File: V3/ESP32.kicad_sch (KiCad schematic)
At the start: 21 parts

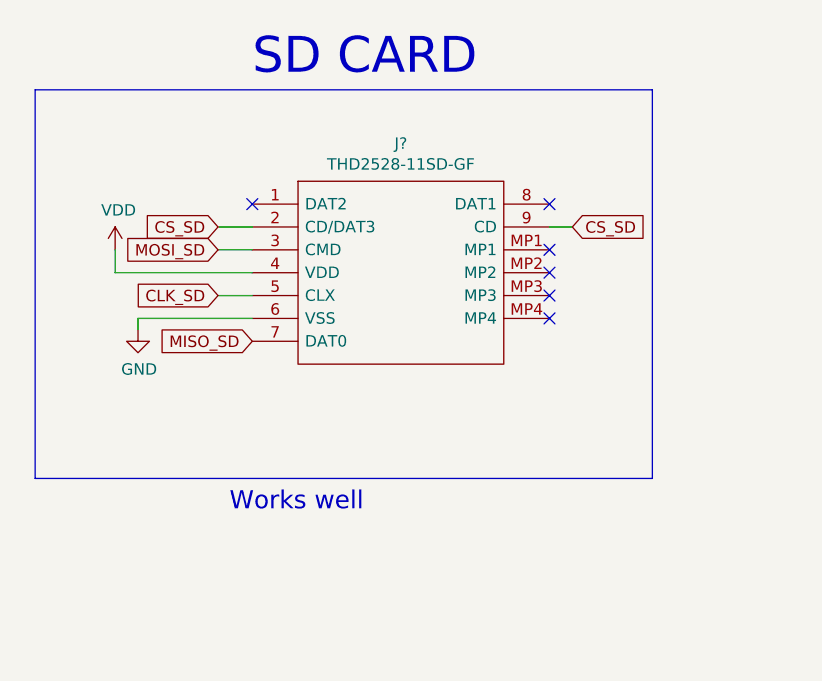
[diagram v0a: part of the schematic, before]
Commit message: Changed imu added flash chip
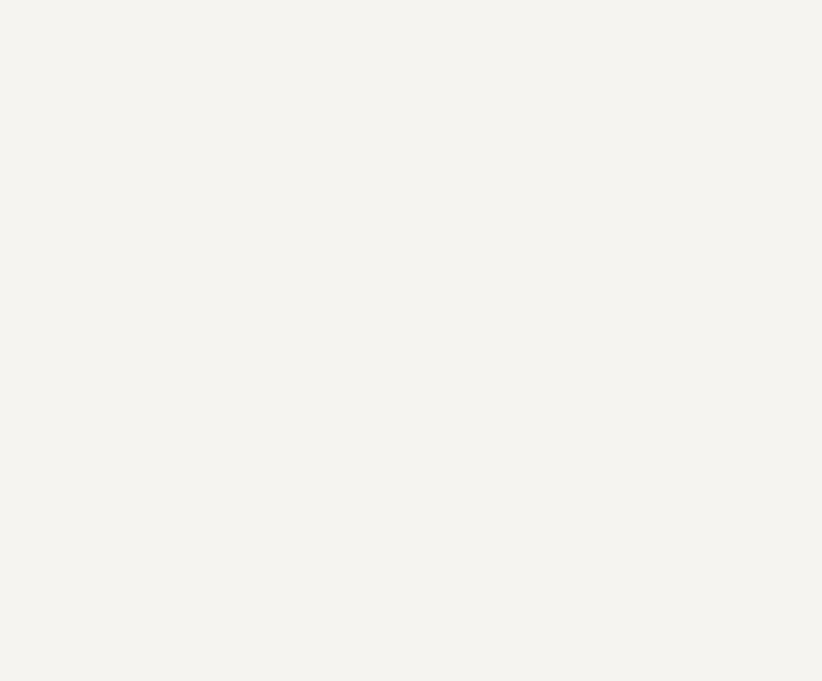
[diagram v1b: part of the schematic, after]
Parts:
- removed J?: THD2528-11SD-GF, footprints:THD252811SDGF, symbol THD2528-11SD-GF:THD2528-11SD-GF
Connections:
- no-connect marks 12 -> 6
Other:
- note removed: "SD CARD"
- note removed: "Works well"
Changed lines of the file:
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@@
   )
   (no_connect (at 179.07 103.505))
-  (no_connect (at 91.44 43.18))
-  (no_connect (at 91.44 35.56))
   (no_connect (at 179.07 90.805))
-  (no_connect (at 58.42 35.56))
   (no_connect (at 179.07 98.425))
   (no_connect (at 179.07 100.965))
   (no_connect (at 179.07 93.345))
   (no_connect (at 179.07 95.885))
-  (no_connect (at 91.44 45.72))
-  (no_connect (at 91.44 40.64))
-  (no_connect (at 91.44 48.26))
   (wire (pts (xy 226.695 50.165) (xy 215.9 50.165))
     (stroke (width 0) (type default) (color 0 0 0 0))
@@
     (stroke (width 0) (type default) (color 0 0 0 0))
   )
-  (polyline (pts (xy 102.87 66.04) (xy 102.87 22.86))
-    (stroke (width 0) (type default) (color 0 0 0 0))
-  )
   (wire (pts (xy 204.47 42.545) (xy 215.9 42.545))
     (stroke (width 0) (type default) (color 0 0 0 0))
   )
-  (polyline (pts (xy 34.29 66.04) (xy 102.87 66.04))
-    (stroke (width 0) (type default) (color 0 0 0 0))
-  )
   (wire (pts (xy 212.09 62.865) (xy 209.55 62.865))
     (stroke (width 0) (type default) (color 0 0 0 0))
@@
     (stroke (width 0) (type default) (color 0 0 0 0))
   )
-  (polyline (pts (xy 34.29 22.86) (xy 34.29 66.04))
-    (stroke (width 0) (type default) (color 0 0 0 0))
-  )
   (polyline (pts (xy 46.355 182.245) (xy 46.355 118.745))
     (stroke (width 0) (type default) (color 0 0 0 0))
   )
-  (polyline (pts (xy 102.87 22.86) (xy 34.29 22.86))
-    (stroke (width 0) (type default) (color 0 0 0 0))
-  )
   (wire (pts (xy 213.36 111.125) (xy 209.55 111.125))
     (stroke (width 0) (type default) (color 0 0 0 0))
@@
     (stroke (width 0) (type default) (color 0 0 0 0))
   )
-  (wire (pts (xy 54.61 45.72) (xy 58.42 45.72))
-    (stroke (width 0) (type default) (color 0 0 0 0))
-  )
   (wire (pts (xy 170.18 60.325) (xy 171.45 60.325))
     (stroke (width 0) (type default) (color 0 0 0 0))
@@
     (stroke (width 0) (type default) (color 0 0 0 0))
   )
-  (wire (pts (xy 43.18 43.18) (xy 58.42 43.18))
-    (stroke (width 0) (type default) (color 0 0 0 0))
-  )
   (wire (pts (xy 212.09 67.945) (xy 209.55 67.945))
     (stroke (width 0) (type default) (color 0 0 0 0))
@@
     (stroke (width 0) (type default) (color 0 0 0 0))
   )
-  (wire (pts (xy 45.72 49.53) (xy 45.72 48.26))
-    (stroke (width 0) (type default) (color 0 0 0 0))
-  )
   (wire (pts (xy 237.49 122.555) (xy 242.57 122.555))
     (stroke (width 0) (type default) (color 0 0 0 0))
@@
     (stroke (width 0) (type default) (color 0 0 0 0))
   )
-  (wire (pts (xy 58.42 40.64) (xy 54.61 40.64))
-    (stroke (width 0) (type default) (color 0 0 0 0))
-  )
   (polyline (pts (xy 108.585 118.745) (xy 108.585 182.245))
     (stroke (width 0) (type default) (color 0 0 0 0))
@@
     (stroke (width 0) (type default) (color 0 0 0 0))
   )
-  (wire (pts (xy 54.61 38.1) (xy 58.42 38.1))
-    (stroke (width 0) (type default) (color 0 0 0 0))
-  )
   (wire (pts (xy 209.55 108.585) (xy 213.36 108.585))
     (stroke (width 0) (type default) (color 0 0 0 0))
@@
     (stroke (width 0) (type default) (color 0 0 0 0))
   )
-  (wire (pts (xy 43.18 40.64) (xy 43.18 43.18))
-    (stroke (width 0) (type default) (color 0 0 0 0))
-  )
   (wire (pts (xy 242.57 128.905) (xy 242.57 130.175))
     (stroke (width 0) (type default) (color 0 0 0 0))
@@
     (stroke (width 0) (type default) (color 0 0 0 0))
   )
-  (wire (pts (xy 91.44 38.1) (xy 93.98 38.1))
-    (stroke (width 0) (type default) (color 0 0 0 0))
-  )
   (wire (pts (xy 209.55 90.805) (xy 212.09 90.805))
     (stroke (width 0) (type default) (color 0 0 0 0))
@@
     (stroke (width 0) (type default) (color 0 0 0 0))
   )
-  (wire (pts (xy 45.72 48.26) (xy 58.42 48.26))
-    (stroke (width 0) (type default) (color 0 0 0 0))
-  )
   (wire (pts (xy 213.36 103.505) (xy 209.55 103.505))
     (stroke (width 0) (type default) (color 0 0 0 0))
-  )
-  (text "SD CARD" (at 58.42 21.59 0)
-    (effects (font (size 3.9878 3.9878)) (justify left bottom))
   )
   (text "Power LED flickers each transmit. There appears to be \na significant voltage drop each transmit.\nVerify with scope. Perhaps use large tantalum cap to supply \ntransmit current. "
@@
     (effects (font (size 3.9878 3.9878)) (justify left bottom))
   )
-  (text "Works well" (at 55.88 69.85 0)
-    (effects (font (size 2.0066 2.0066)) (justify left bottom))
-  )
   (text "800uV resolution :0\n(Theoretically)" (at 226.06 127.635 0)
     (effects (font (size 0.9906 0.9906)) (justify left bottom))
@@
     (effects (font (size 1.27 1.27)) (justify right))
     (property "Intersheet References" "${INTERSHEET_REFS}" (id 0) (at 124.46 -6.985 0)
-      (effects (font (size 1.27 1.27)) hide)
-    )
-  )
-  (global_label "CLK_SD" (shape input) (at 54.61 45.72 180) (fields_autoplaced)
-    (effects (font (size 1.27 1.27)) (justify right))
-    (property "Intersheet References" "${INTERSHEET_REFS}" (id 0) (at -191.77 -83.82 0)
       (effects (font (size 1.27 1.27)) hide)
     )
@@
     )
   )
-  (global_label "MOSI_SD" (shape input) (at 54.61 40.64 180) (fields_autoplaced)
-    (effects (font (size 1.27 1.27)) (justify right))
-    (property "Intersheet References" "${INTERSHEET_REFS}" (id 0) (at -191.77 -83.82 0)
-      (effects (font (size 1.27 1.27)) hide)
-    )
-  )
   (global_label "RXD2_GPS" (shape input) (at 213.36 118.745 0) (fields_autoplaced)
     (effects (font (size 1.27 1.27)) (justify left))
@@
     )
   )
-  (global_label "CS_SD" (shape input) (at 93.98 38.1 0) (fields_autoplaced)
-    (effects (font (size 1.27 1.27)) (justify left))
-    (property "Intersheet References" "${INTERSHEET_REFS}" (id 0) (at -191.77 -83.82 0)
-      (effects (font (size 1.27 1.27)) hide)
-    )
-  )
   (global_label "MISO_RF" (shape input) (at 212.09 75.565 0) (fields_autoplaced)
     (effects (font (size 1.27 1.27)) (justify left))
@@
     )
   )
-  (global_label "CS_SD" (shape input) (at 54.61 38.1 180) (fields_autoplaced)
-    (effects (font (size 1.27 1.27)) (justify right))
-    (property "Intersheet References" "${INTERSHEET_REFS}" (id 0) (at -191.77 -83.82 0)
-      (effects (font (size 1.27 1.27)) hide)
-    )
-  )
   (global_label "CS_SD" (shape input) (at 212.09 73.025 0) (fields_autoplaced)
     (effects (font (size 1.27 1.27)) (justify left))
@@
       (effects (font (size 1.27 1.27)) hide)
     )
-  )
-  (global_label "MISO_SD" (shape input) (at 58.42 50.8 180) (fields_autoplaced)
-    (effects (font (size 1.27 1.27)) (justify right))
-    (property "Intersheet References" "${INTERSHEET_REFS}" (id 0) (at -191.77 -83.82 0)
-      (effects (font (size 1.27 1.27)) hide)
-    )
-  )
-  (symbol (lib_id "power:VDD") (at 43.18 40.64 0) (unit 1)
-    (in_bom yes) (on_board yes)
-    (property "Reference" "#PWR?" (id 0) (at 43.18 44.45 0)
-      (effects (font (size 1.27 1.27)) hide)
-    )
-    (property "Value" "VDD" (id 1) (at 43.561 36.2458 0))
-    (property "Footprint" "" (id 2) (at 43.18 40.64 0)
-      (effects (font (size 1.27 1.27)) hide)
-    )
-    (property "Datasheet" "" (id 3) (at 43.18 40.64 0)
-      (effects (font (size 1.27 1.27)) hide)
-    )
-    (pin "1")
   )
   (symbol (lib_id "power:VDD") (at 226.06 86.995 0) (unit 1)
@@
     )
     (property "Datasheet" "" (id 3) (at 226.06 86.995 0)
-      (effects (font (size 1.27 1.27)) hide)
-    )
-    (pin "1")
-  )
-  (symbol (lib_id "power:GND") (at 45.72 49.53 0) (unit 1)
-    (in_bom yes) (on_board yes)
-    (property "Reference" "#PWR?" (id 0) (at 45.72 55.88 0)
-      (effects (font (size 1.27 1.27)) hide)
-    )
-    (property "Value" "GND" (id 1) (at 45.847 53.9242 0))
-    (property "Footprint" "" (id 2) (at 45.72 49.53 0)
-      (effects (font (size 1.27 1.27)) hide)
-    )
-    (property "Datasheet" "" (id 3) (at 45.72 49.53 0)
       (effects (font (size 1.27 1.27)) hide)
     )
@@
     (pin "2")
   )
-  (symbol (lib_id "THD2528-11SD-GF:THD2528-11SD-GF") (at 58.42 35.56 0) (unit 1)
-    (in_bom yes) (on_board yes)
-    (property "Reference" "J?" (id 0) (at 74.93 28.829 0))
-    (property "Value" "THD2528-11SD-GF" (id 1) (at 74.93 31.1404 0))
-    (property "Footprint" "footprints:THD252811SDGF" (id 2) (at 87.63 33.02 0)
-      (effects (font (size 1.27 1.27)) (justify left) hide)
-    )
-    (property "Datasheet" "https://datasheet.lcsc.com/szlcsc/1903291130_THD-THD2528-11SD-GF_C283232.pdf" (id 3) (at 87.63 35.56 0)
-      (effects (font (size 1.27 1.27)) (justify left) hide)
-    )
-    (property "Description" "Connector - Card Sockets SMD RoHS" (id 4) (at 87.63 38.1 0)
-      (effects (font (size 1.27 1.27)) (justify left) hide)
-    )
-    (property "Height" "2" (id 5) (at 87.63 40.64 0)
-      (effects (font (size 1.27 1.27)) (justify left) hide)
-    )
-    (property "Manufacturer_Name" "THD" (id 6) (at 87.63 43.18 0)
-      (effects (font (size 1.27 1.27)) (justify left) hide)
-    )
-    (property "Manufacturer_Part_Number" "THD2528-11SD-GF" (id 7) (at 87.63 45.72 0)
-      (effects (font (size 1.27 1.27)) (justify left) hide)
-    )
-    (property "Mouser Part Number" "" (id 8) (at 87.63 48.26 0)
-      (effects (font (size 1.27 1.27)) (justify left) hide)
-    )
-    (property "Mouser Price/Stock" "" (id 9) (at 87.63 50.8 0)
-      (effects (font (size 1.27 1.27)) (justify left) hide)
-    )
-    (property "Arrow Part Number" "" (id 10) (at 87.63 53.34 0)
-      (effects (font (size 1.27 1.27)) (justify left) hide)
-    )
-    (property "Arrow Price/Stock" "" (id 11) (at 87.63 55.88 0)
-      (effects (font (size 1.27 1.27)) (justify left) hide)
-    )
-    (pin "1")
-    (pin "2")
-    (pin "3")
-    (pin "4")
-    (pin "5")
-    (pin "6")
-    (pin "7")
-    (pin "8")
-    (pin "9")
-    (pin "MP1")
-    (pin "MP2")
-    (pin "MP3")
-    (pin "MP4")
-  )
   (symbol (lib_id "Device:R_Small") (at 242.57 55.245 0) (unit 1)

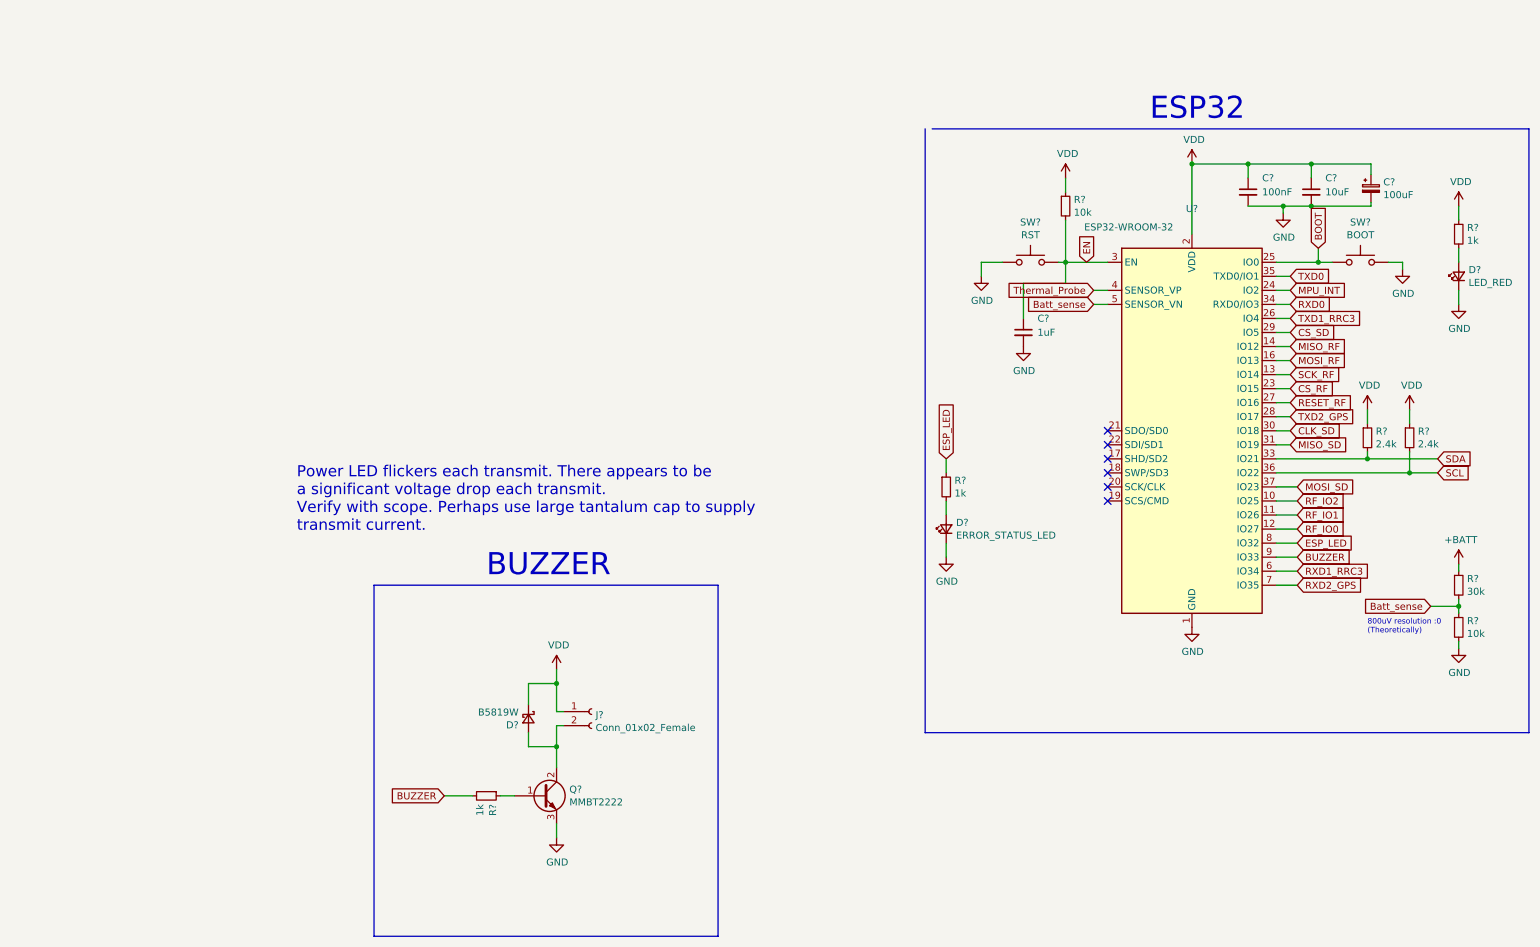
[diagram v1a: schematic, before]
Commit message: Added sims, updated V3 board
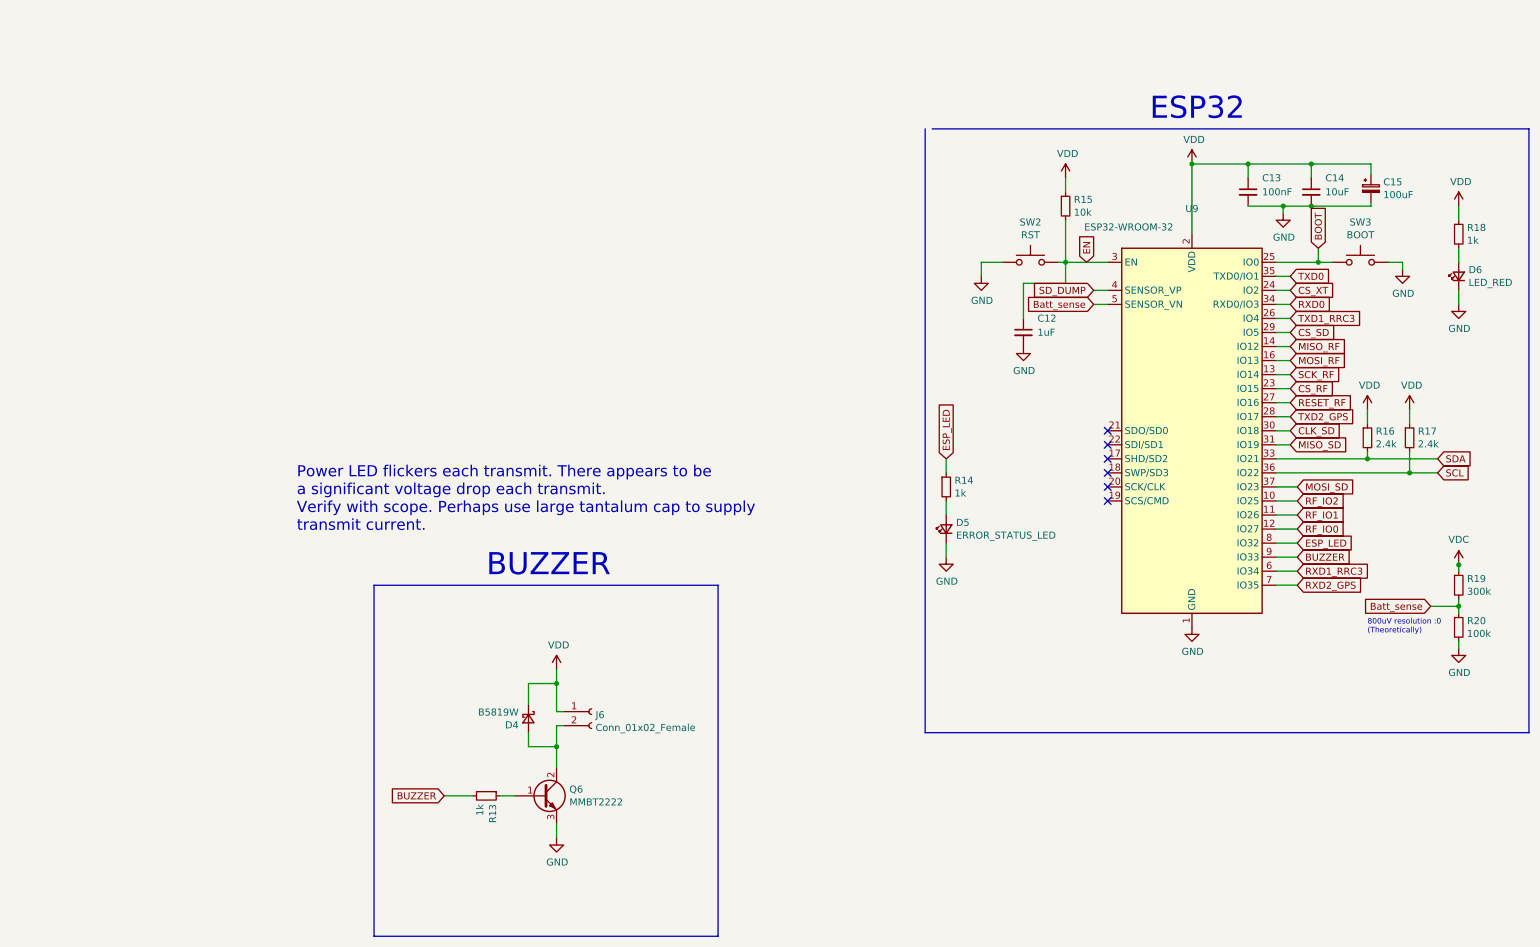
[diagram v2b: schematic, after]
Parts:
- R19: renamed from R?; value 30k -> 300k
- R20: renamed from R?; value 10k -> 100k
- gave numbers to parts that had none: 18
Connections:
- net +BATT renamed VDC
- net MPU_INT renamed CS_XT
- net Thermal_Probe renamed SD_DUMP
